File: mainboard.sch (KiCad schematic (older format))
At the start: 56 parts

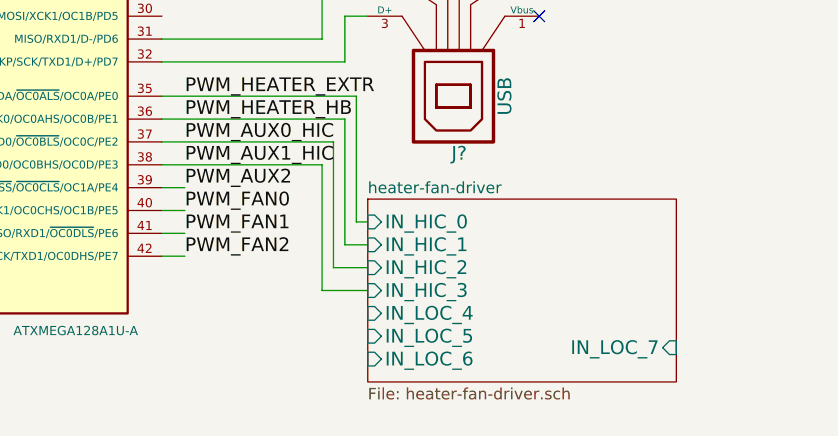
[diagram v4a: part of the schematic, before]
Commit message: Added signal LEDs to hi-current and lo-current drivers, updated BOM
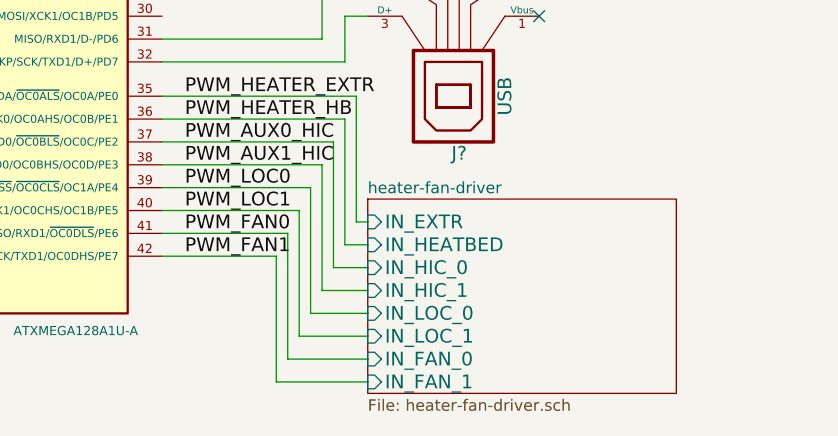
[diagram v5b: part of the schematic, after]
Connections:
- net PWM_FAN2 is gone; now on net PWM_FAN1: IC?.42 (EVOUT/CLKP/SCK/TXD1/OC0DHS/PE7)
- net PWM_FAN0: now also IC?.41 (MISO/RXD1/~OC0DLS~/PE6); no longer IC?.40 (MOSI/XCK1/OC0CHS/OC1B/PE5)
- net PWM_FAN1: no longer IC?.41 (MISO/RXD1/~OC0DLS~/PE6)
- net PWM_AUX2 renamed PWM_LOC0
- new net PWM_LOC1: IC?.40 (MOSI/XCK1/OC0CHS/OC1B/PE5)
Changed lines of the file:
@@
 	0    1    1    0
 $EndComp
+Text Label 4200 7000 0    60   ~ 0
+PWM_FAN1
+Text Label 4200 6800 0    60   ~ 0
+PWM_LOC1
 Text Label 4200 6900 0    60   ~ 0
-PWM_FAN1
-Text Label 4200 7000 0    60   ~ 0
-PWM_FAN2
-Text Label 4200 6800 0    60   ~ 0
 PWM_FAN0
 Text Label 4200 6400 0    60   ~ 0
@@
 PWM_AUX1_HIC
 Text Label 4200 6700 0    60   ~ 0
-PWM_AUX2
+PWM_LOC0
 Text Notes 4550 4050 0    60   ~ 0
 Input from\nEndstops
@@
 	1650 2200 1650 2300
 Wire Wire Line
-	4200 6900 4100 6900
-Wire Wire Line
-	4200 6800 4100 6800
-Wire Wire Line
-	4200 6700 4100 6700
+	4100 6900 4650 6900
+Wire Wire Line
+	4100 6800 4700 6800
+Wire Wire Line
+	4100 6700 4750 6700
 Wire Wire Line
 	4100 6600 4800 6600
@@
 	8750 4900 8550 4900
 Wire Wire Line
-	4200 7000 4100 7000
+	4100 7000 4600 7000
 Text Label 4200 6500 0    60   ~ 0
 PWM_AUX0_HIC
@@
 	1    0    0    -1
 $EndComp
-$Sheet
-S 5000 6750 1350 800
-U 534EA8E8
-F0 "heater-fan-driver" 50
-F1 "heater-fan-driver.sch" 50
-F2 "IN_HIC_0" I L 5000 6850 60
-F3 "IN_HIC_1" I L 5000 6950 60
-F4 "IN_HIC_2" I L 5000 7050 60
-F5 "IN_HIC_3" I L 5000 7150 60
-F6 "IN_LOC_4" I L 5000 7250 60
-F7 "IN_LOC_5" I L 5000 7350 60
-F8 "IN_LOC_6" I L 5000 7450 60
-F9 "IN_LOC_7" I R 6350 7400 60
-$EndSheet
 Wire Wire Line
 	4950 6300 4950 6850
@@
 	1    0    0    -1
 $EndComp
+Wire Wire Line
+	4750 6700 4750 7250
+Wire Wire Line
+	4750 7250 5000 7250
+Wire Wire Line
+	4700 6800 4700 7350
+Wire Wire Line
+	4700 7350 5000 7350
+Wire Wire Line
+	4650 6900 4650 7450
+Wire Wire Line
+	4650 7450 5000 7450
+Wire Wire Line
+	4600 7000 4600 7550
+Wire Wire Line
+	4600 7550 5000 7550
+$Sheet
+S 5000 6750 1350 850
+U 534EA8E8
+F0 "heater-fan-driver" 50
+F1 "heater-fan-driver.sch" 50
+F2 "IN_FAN_0" I L 5000 7450 60
+F3 "IN_FAN_1" I L 5000 7550 60
+F4 "IN_LOC_0" I L 5000 7250 60
+F5 "IN_LOC_1" I L 5000 7350 60
+F6 "IN_EXTR" I L 5000 6850 60
+F7 "IN_HEATBED" I L 5000 6950 60
+F8 "IN_HIC_0" I L 5000 7050 60
+F9 "IN_HIC_1" I L 5000 7150 60
+$EndSheet
 $EndSCHEMATC

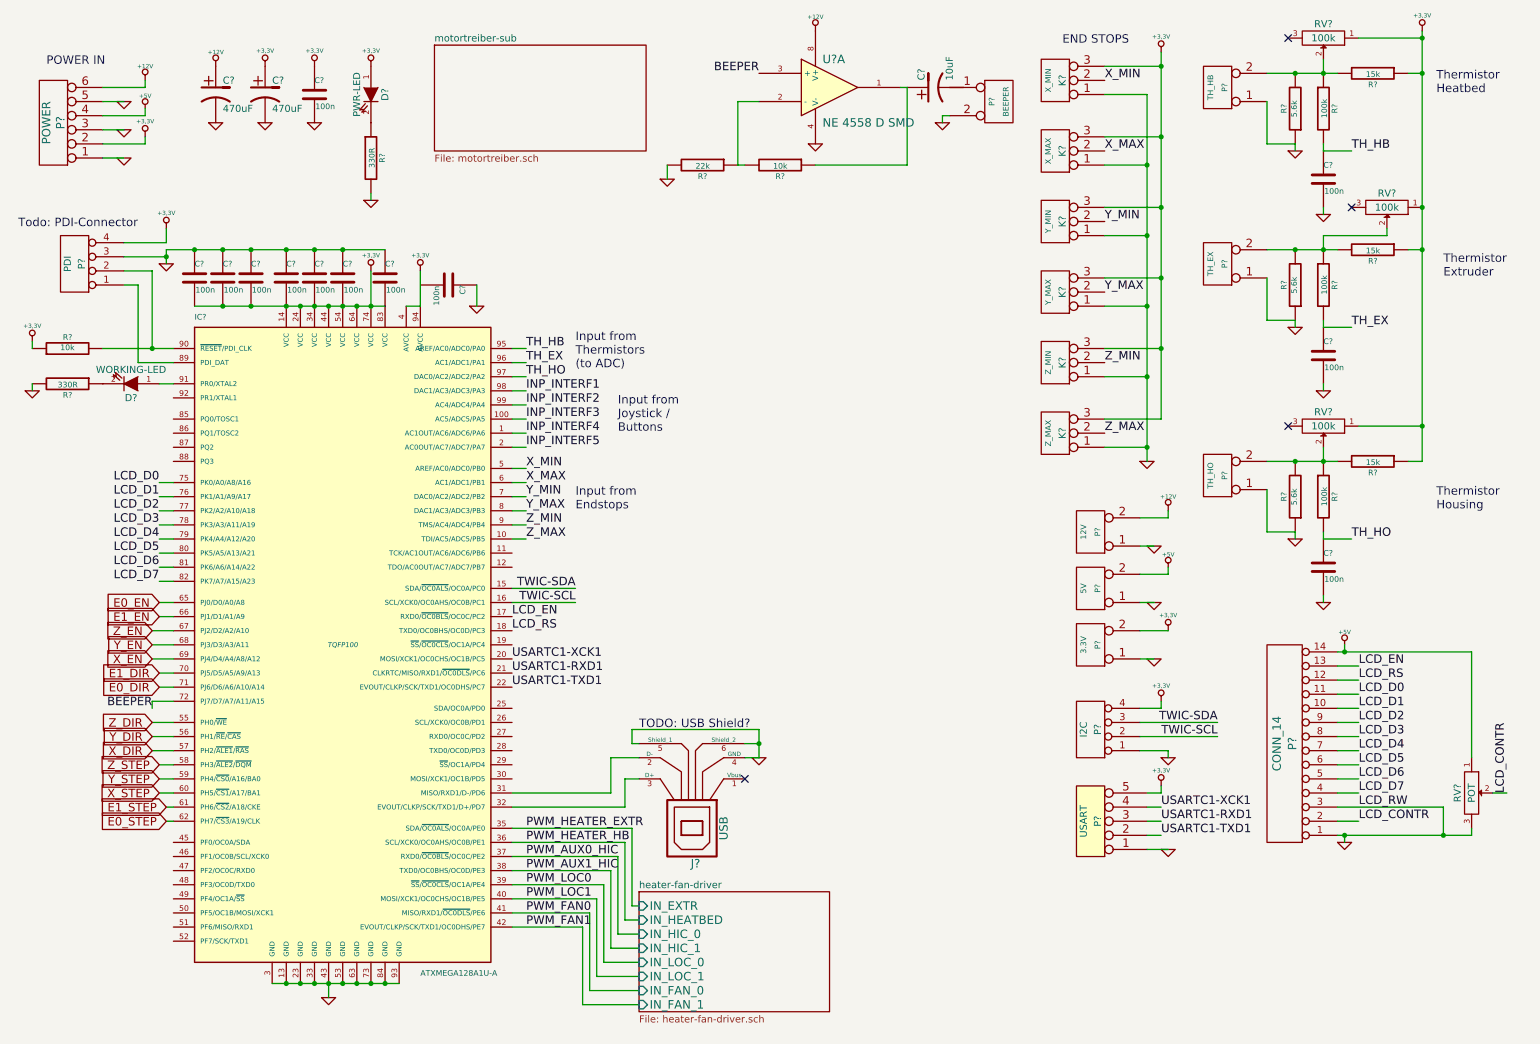
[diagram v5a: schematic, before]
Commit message: Added Open Collector connector for future expansion
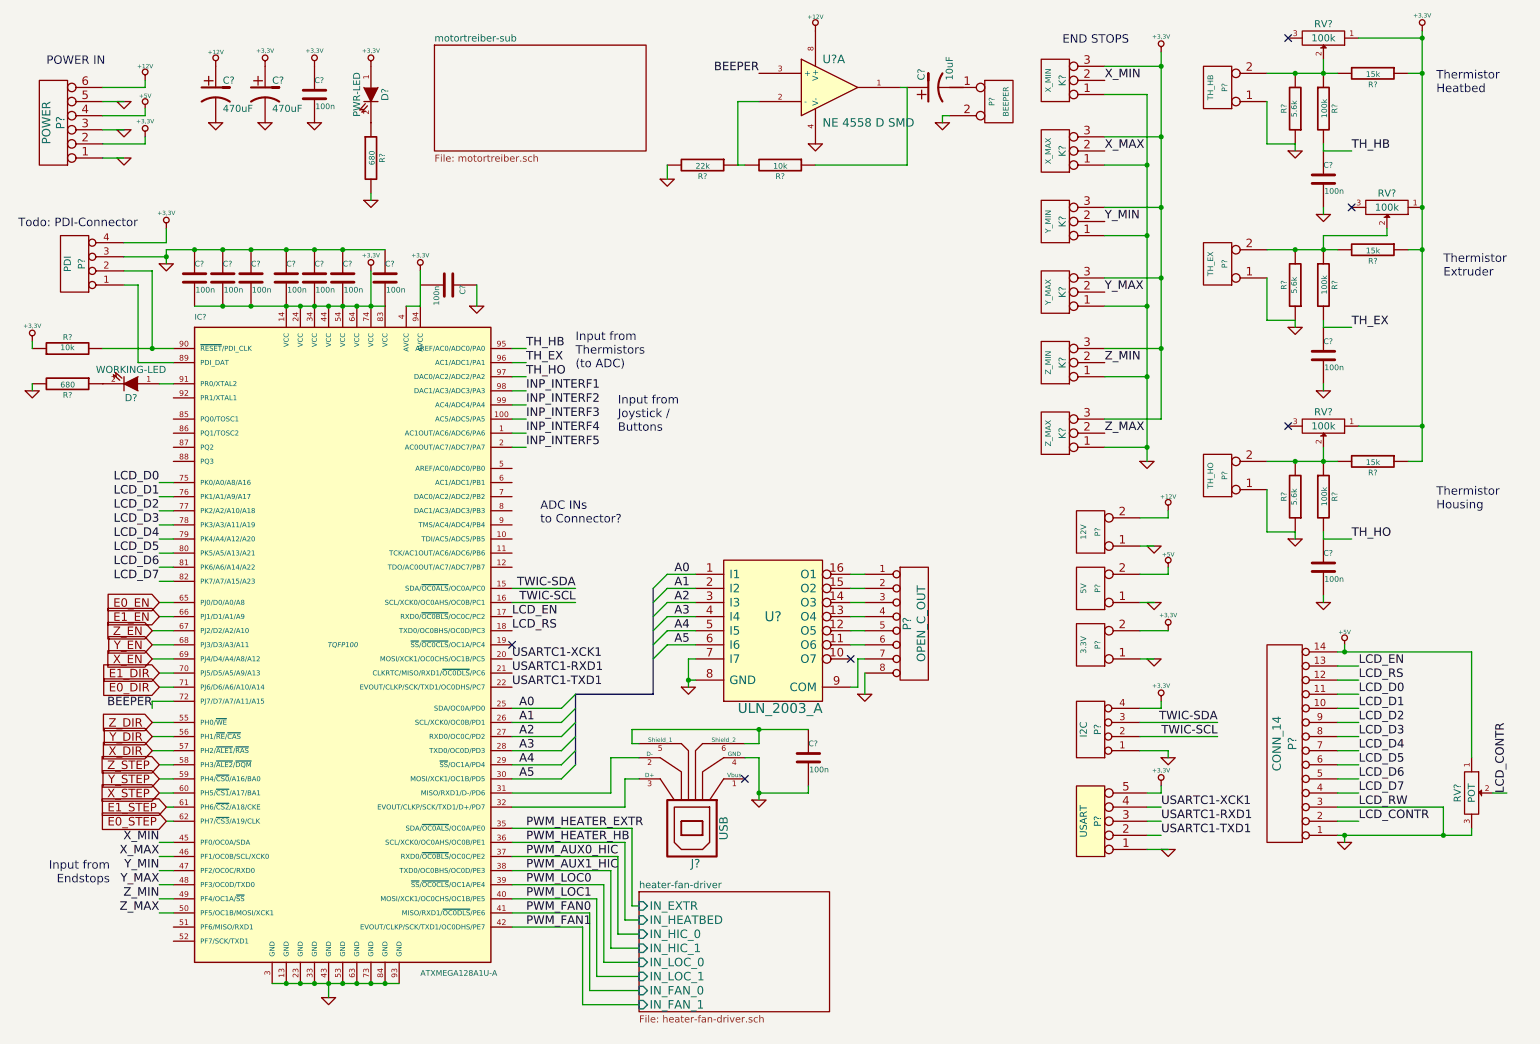
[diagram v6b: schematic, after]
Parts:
- added C?: 100n, symbol C
- added P?: OPEN_C_OUT, symbol CONN_8
- added U?: ULN_2003_A, symbol ULN_2003_A
- R? (x2): value 330R -> 680
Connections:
- net GND: now also C?.2, P?.8 (P8), U?.7 (I7), U?.8 (GND); no longer J?.5 (Shield_1), J?.6 (Shield_2)
- net X_MAX: now also IC?.46 (PF1/OC0B/SCL/XCK0); no longer IC?.6 (AC1/ADC1/PB1)
- net X_MIN: now also IC?.45 (PF0/OC0A/SDA); no longer IC?.5 (AREF/AC0/ADC0/PB0)
- net Y_MAX: now also IC?.48 (PF3/OC0D/TXD0); no longer IC?.8 (DAC1/AC3/ADC3/PB3)
- net Y_MIN: now also IC?.47 (PF2/OC0C/RXD0); no longer IC?.7 (DAC0/AC2/ADC2/PB2)
- net Z_MAX: now also IC?.50 (PF5/OC1B/MOSI/XCK1); no longer IC?.10 (TDI/AC5/ADC5/PB5)
- net Z_MIN: now also IC?.49 (PF4/OC1A/~SS~); no longer IC?.9 (TMS/AC4/ADC4/PB4)
- net A0: now reaches IC?.25 (SDA/OC0A/PD0)
- net A0: now also U?.1 (I1)
- net A1: now reaches IC?.26 (SCL/XCK0/OC0B/PD1)
- net A1: now also U?.2 (I2)
- net A2: now reaches IC?.27 (RXD0/OC0C/PD2)
- net A2: now also U?.3 (I3)
- net A3: now reaches IC?.28 (TXD0/OC0D/PD3)
- net A3: now also U?.4 (I4)
- net A4: now reaches IC?.29 (~SS~/OC1A/PD4)
- net A4: now also U?.5 (I5)
- net A5: now reaches IC?.30 (MOSI/XCK1/OC1B/PD5)
- net A5: now also U?.6 (I6)
- new net: C?.1, J?.5 (Shield_1), J?.6 (Shield_2)
- new net: P?.6 (P6), U?.11 (O6)
- new net: P?.5 (P5), U?.12 (O5)
- new net: P?.4 (P4), U?.13 (O4)
- new net: P?.3 (P3), U?.14 (O3)
- new net: P?.2 (P2), U?.15 (O2)
- new net: P?.1 (P1), U?.16 (O1)
- new net: P?.7 (P7), U?.9 (COM)
- no-connect marks 4 -> 6
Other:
- note added: "ADC INs\nto Connector?"
- note removed: "TODO: USB Shield?"

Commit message: Added potentiometer to make beeper volume adjustable
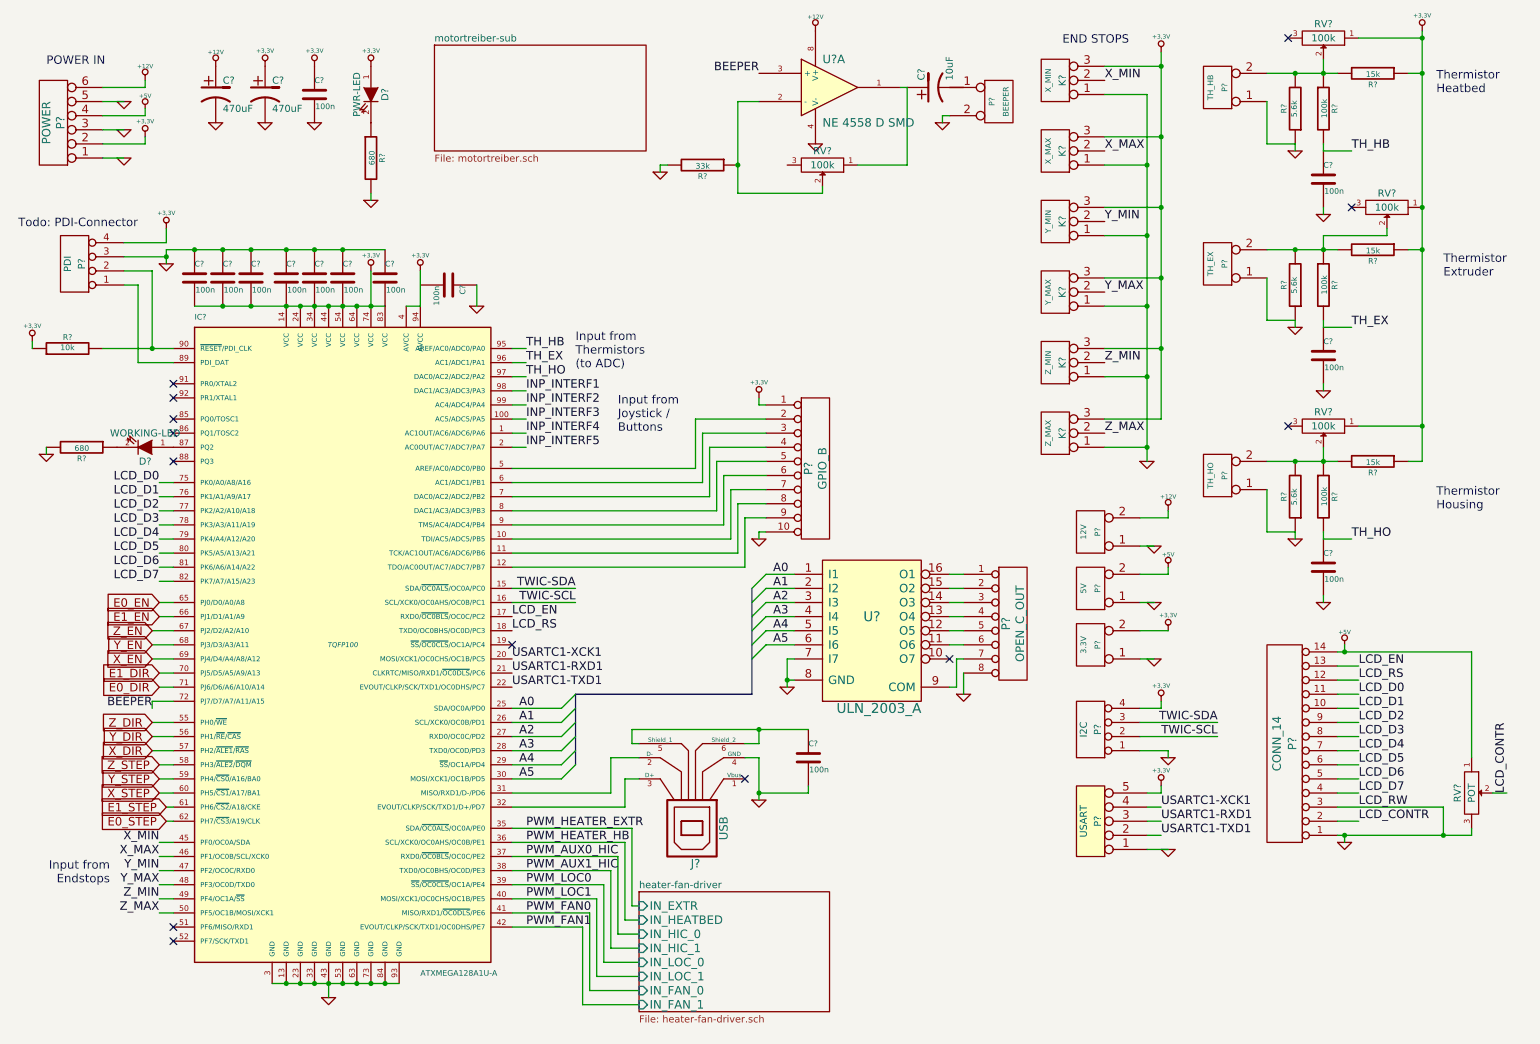
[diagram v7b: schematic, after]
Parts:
- removed R?: 22k, symbol R
- added P?: GPIO_B, symbol CONN_10
- added RV?: 100k, symbol POT
- R?: value 10k -> 33k
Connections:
- net +3.3V: now also P?.1 (P1)
- net GND: now also R?.2, P?.10 (P10)
- net at D?.1 (A): now also IC?.87 (PQ2); no longer IC?.91 (PR0/XTAL2)
- net at C?.1, U?.1: now also RV?.1; no longer R?.1
- net at U?.2 (-): now also R?.1, RV?.2; no longer R?.2
- net at IC?.10 (TDI/AC5/ADC5/PB5): now also P?.7 (P7)
- net at IC?.11 (TCK/AC1OUT/AC6/ADC6/PB6): now also P?.8 (P8)
- net at IC?.12 (TDO/AC0OUT/AC7/ADC7/PB7): now also P?.9 (P9)
- net at IC?.5 (AREF/AC0/ADC0/PB0): now also P?.2 (P2)
- net at IC?.6 (AC1/ADC1/PB1): now also P?.3 (P3)
- net at IC?.7 (DAC0/AC2/ADC2/PB2): now also P?.4 (P4)
- net at IC?.8 (DAC1/AC3/ADC3/PB3): now also P?.5 (P5)
- net at IC?.9 (TMS/AC4/ADC4/PB4): now also P?.6 (P6)
- no-connect marks 6 -> 13
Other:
- note removed: "ADC INs\nto Connector?"
- moved on the sheet: D?, P?, R?, U?
